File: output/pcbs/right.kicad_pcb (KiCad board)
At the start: 2 copper layers, 140.2 x 118.9 mm, 62 parts

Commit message: PCB config is now mostly completed
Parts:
- moved D1 264.6 mm to (364.6, 88.0)
- moved D2 264.6 mm to (364.6, 71.0)
- moved D3 264.6 mm to (364.6, 54.0)
- moved D4 264.6 mm to (364.6, 37.0)
- moved S1 264.6 mm to (364.6, 83.0)
- moved S2 264.6 mm to (364.6, 66.0)
- moved S3 264.6 mm to (364.6, 49.0)
- moved S4 264.6 mm to (364.6, 32.0)
- moved D5 219.6 mm to (342.1, 88.0)
- moved D6 219.6 mm to (342.1, 71.0)
- moved D7 219.6 mm to (342.1, 54.0)
- moved D8 219.6 mm to (342.1, 37.0)
- moved S5 219.6 mm to (342.1, 83.0)
- moved S6 219.6 mm to (342.1, 66.0)
- moved S7 219.6 mm to (342.1, 49.0)
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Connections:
- net extra_cluster renamed mirror_extra_cluster
- net index_bottom renamed mirror_index_bottom
- net index_home renamed mirror_index_home
- net index_mod renamed mirror_index_mod
- net index_num renamed mirror_index_num
- net index_top renamed mirror_index_top
- net inner_bottom renamed mirror_inner_bottom
- net inner_home renamed mirror_inner_home
- net inner_num renamed mirror_inner_num
- net inner_top renamed mirror_inner_top
- net middle_bottom renamed mirror_middle_bottom
- net middle_home renamed mirror_middle_home
- net middle_mod renamed mirror_middle_mod
- net middle_num renamed mirror_middle_num
- net middle_top renamed mirror_middle_top
- net outer_bottom renamed mirror_outer_bottom
- net outer_home renamed mirror_outer_home
- net outer_num renamed mirror_outer_num
- net outer_top renamed mirror_outer_top
- net pinky_bottom renamed mirror_pinky_bottom
- net pinky_home renamed mirror_pinky_home
- net pinky_num renamed mirror_pinky_num
- net pinky_top renamed mirror_pinky_top
- net ring_bottom renamed mirror_ring_bottom
- net ring_home renamed mirror_ring_home
- net ring_mod renamed mirror_ring_mod
- net ring_num renamed mirror_ring_num
- net ring_top renamed mirror_ring_top
- net space_cluster renamed mirror_space_cluster
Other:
- outline, holes or cut-outs redrawn

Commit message: A bit more touch-up on the PCB.  Things are shaping up, but not yet done.
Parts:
- added ROT1: , rotary_encoder, F.Cu at (251.6, 70.5)
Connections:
- D28 pad 1: (no net) -> P113
- D29 pad 1: (no net) -> P113
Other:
- board text added: "CYBERFOX-60"
- board text removed: "CYBERFOX"

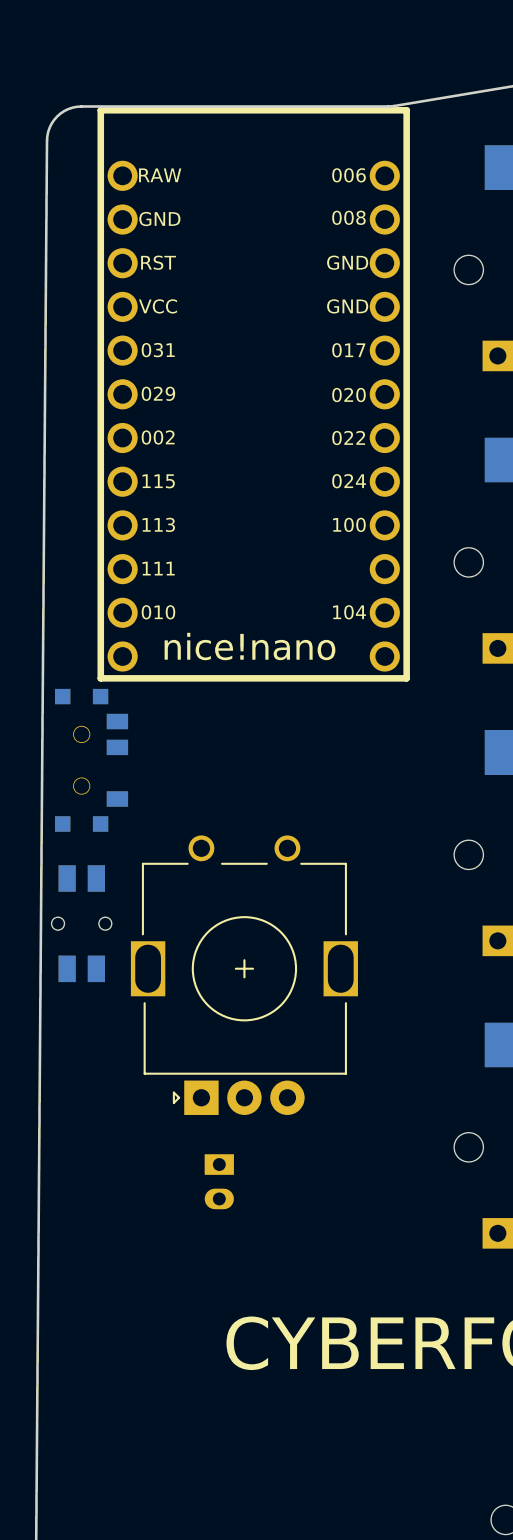
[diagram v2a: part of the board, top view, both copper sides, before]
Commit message: Changed from rotary knob to scrollwheel. Further minor refinements.
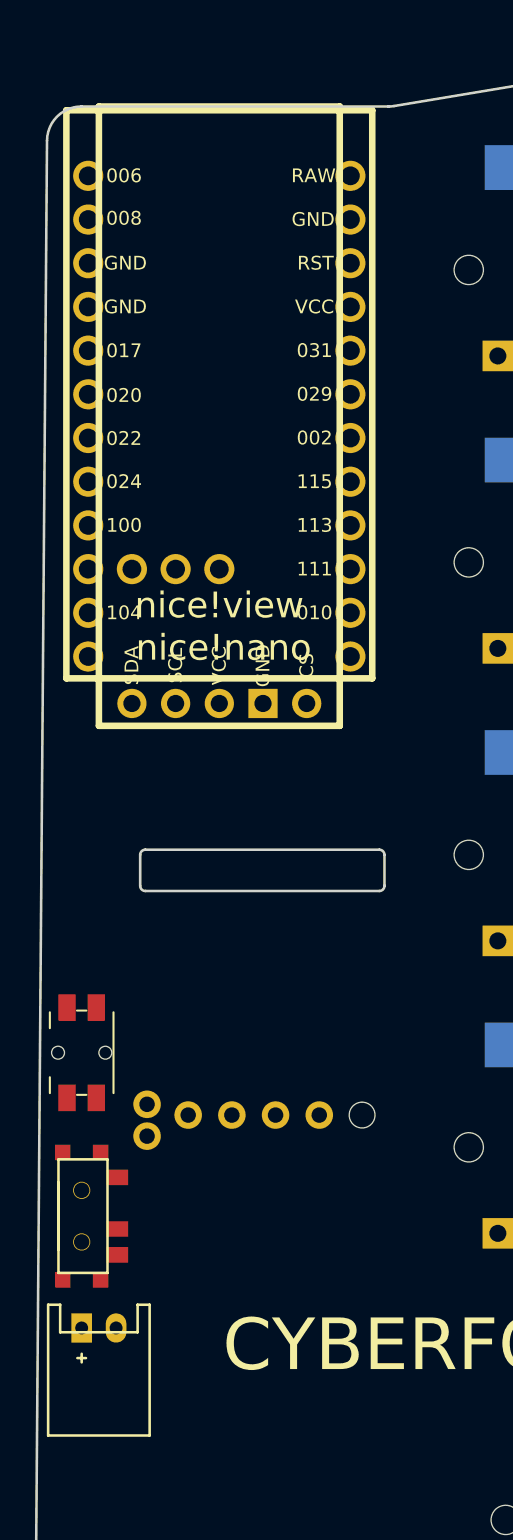
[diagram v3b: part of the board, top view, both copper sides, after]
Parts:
- removed ROT1: , rotary_encoder
- added REF**: RollerEncoder_Panasonic_EVQWGD001, RollerEncoder_Panasonic_EVQWGD001, F.Cu at (252.1, 73.5)
- added niceView1: niceView, lib:niceView_headers, F.Cu at (250.1, 56.5)
- moved T1 26.5 mm to (242.1, 85.0)
- moved JST1 11.0 mm to (243.1, 91.5), turned to 0 degrees
- moved B1 7.50 mm to (242.1, 75.5)
- moved MCU1 2.00 mm to (250.1, 38.5)
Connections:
- net pos renamed POS
- D13 pad 1: P013 -> P031
- D18 pad 1: P013 -> P031
- D23 pad 1: P013 -> P031
- D27 pad 1: P013 -> P031
- D4 pad 1: P013 -> P031
- D8 pad 1: P013 -> P031
- S1 pad 1: P020 -> P011
- S10 pad 1: P024 -> P106
- S11 pad 1: P024 -> P106
- S12 pad 1: P024 -> P106
- S13 pad 1: P024 -> P106
- S14 pad 1: P024 -> P106
- S15 pad 1: P100 -> P111
- S16 pad 1: P100 -> P111
- S17 pad 1: P100 -> P111
- S18 pad 1: P100 -> P111
- S19 pad 1: P100 -> P111
- S2 pad 1: P020 -> P011
- S20 pad 1: P011 -> P010
- S21 pad 1: P011 -> P010
- S22 pad 1: P011 -> P010
- S23 pad 1: P011 -> P010
- S24 pad 1: P017 -> P009
- S25 pad 1: P017 -> P009
- S26 pad 1: P017 -> P009
- S27 pad 1: P017 -> P009
- S28 pad 1: P011 -> P010
- S29 pad 1: P017 -> P009
- S3 pad 1: P020 -> P011
- S4 pad 1: P020 -> P011
- S5 pad 1: P022 -> P104
- S6 pad 1: P022 -> P104
- S7 pad 1: P022 -> P104
- S8 pad 1: P022 -> P104
- S9 pad 1: P022 -> P104

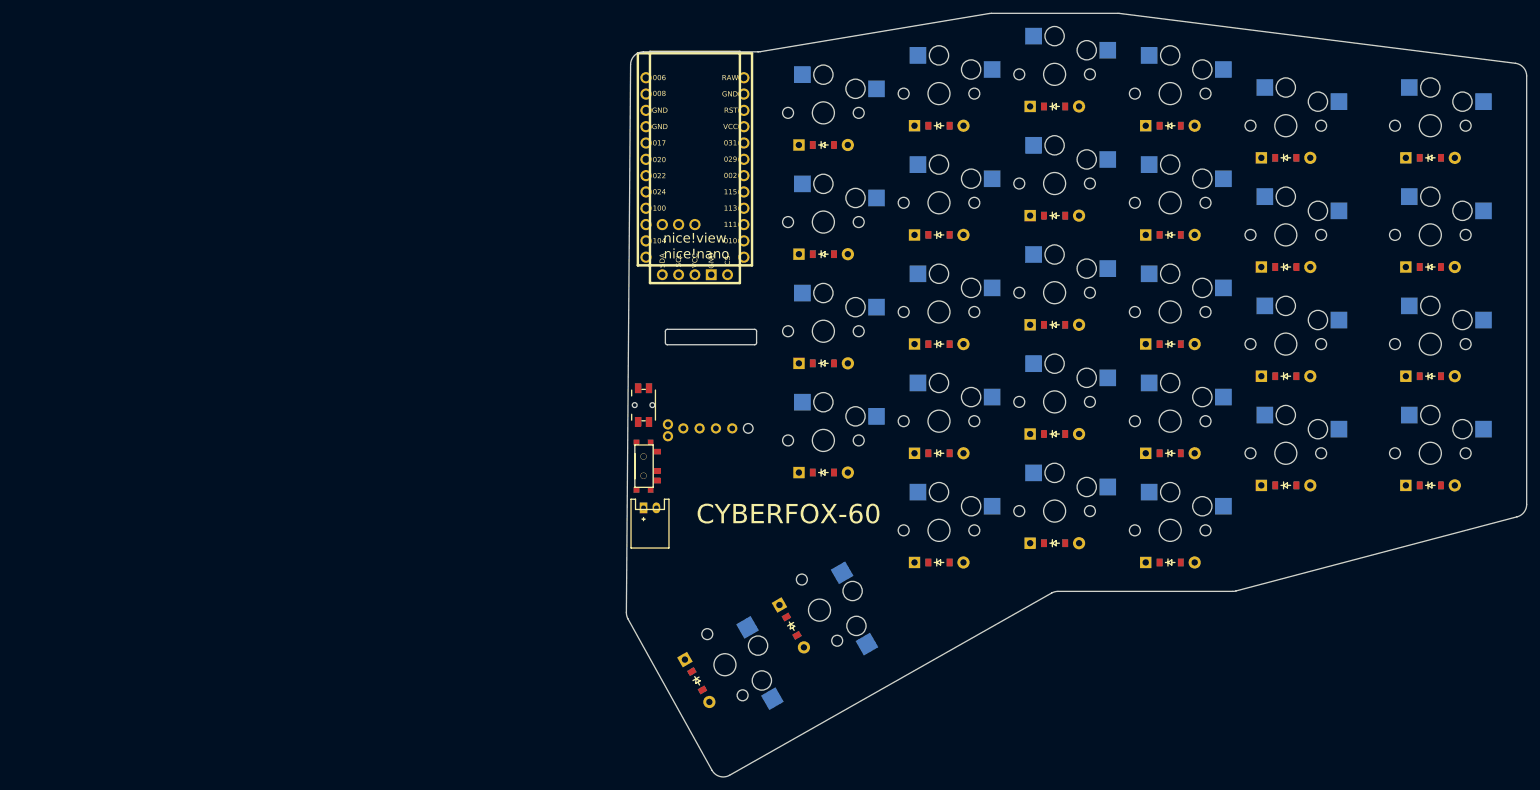
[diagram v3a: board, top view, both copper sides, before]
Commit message: Added screw holes and an extra diode for the scrollwheel
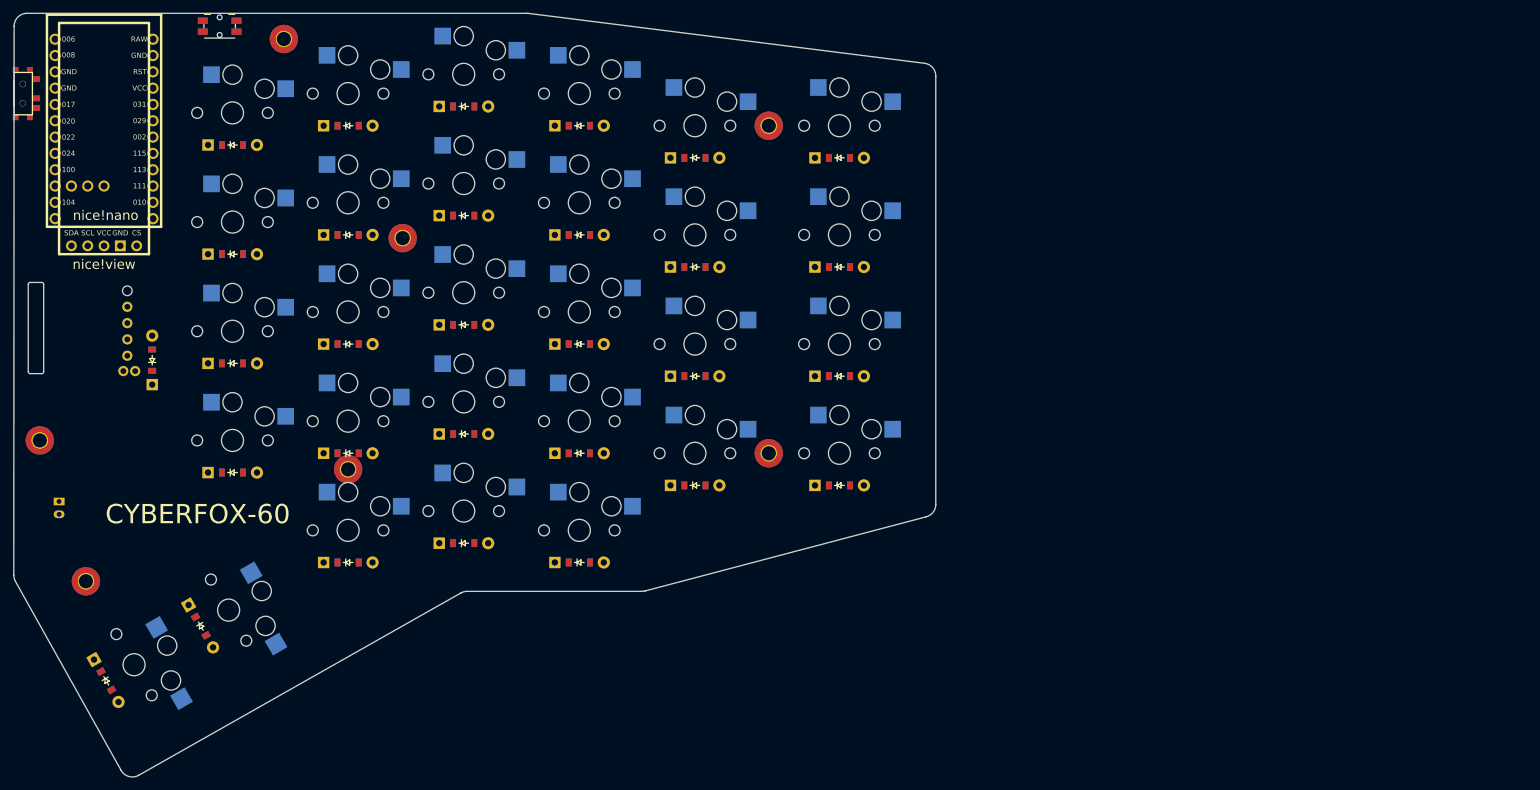
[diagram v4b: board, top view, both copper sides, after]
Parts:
- added D30: , ComboDiode, F.Cu at (165.6, 68.5)
- added _2: , HOLE_M2, F.Cu at (155.3, 102.9)
- added _3: , HOLE_M2, F.Cu at (148.1, 81.0)
- added _4: , HOLE_M2, F.Cu at (186.1, 18.5)
- added _5: , HOLE_M2, F.Cu at (261.6, 32.0)
- added _6: , HOLE_M2, F.Cu at (261.6, 83.0)
- added _7: , HOLE_M2, F.Cu at (204.6, 49.5)
- added _8: , HOLE_M2, F.Cu at (196.1, 85.5)
- REF**: value RollerEncoder_Panasonic_EVQWGD001 -> EVQWGD001
- moved T1 112.7 mm to (145.5, 27.0)
- moved REF** 96.5 mm to (156.1, 64.0), turned to -180 degrees
- moved MCU1 92.2 mm to (158.1, 32.5)
- moved niceView1 92.1 mm to (158.1, 52.0)
- moved D1 92.0 mm to (272.6, 88.0)
- moved D10 92.0 mm to (232.1, 83.0)
- moved D11 92.0 mm to (232.1, 66.0)
- moved D12 92.0 mm to (232.1, 49.0)
- moved D13 92.0 mm to (232.1, 32.0)
- moved D14 92.0 mm to (214.1, 97.0)
- moved D15 92.0 mm to (214.1, 80.0)
- moved D16 92.0 mm to (214.1, 63.0)
- moved D17 92.0 mm to (214.1, 46.0)
- moved D18 92.0 mm to (214.1, 29.0)
- moved D19 92.0 mm to (196.1, 100.0)
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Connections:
- REF** pad S2: P113 -> ROTARY
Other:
- board size 140.2 x 118.9 mm -> 143.6 x 118.9 mm

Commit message: Starting to trace the PCB
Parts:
- moved _8 47.3 mm to (231.9, 116.5)
- moved D1 39.1 mm to (310.6, 97.2)
- moved D5 39.1 mm to (288.1, 97.2)
- moved S1 39.1 mm to (310.6, 92.2)
- moved S5 39.1 mm to (288.1, 92.2)
- moved D2 38.9 mm to (310.6, 79.5)
- moved D6 38.9 mm to (288.1, 79.5)
- moved S2 38.9 mm to (310.6, 74.5)
- moved S6 38.9 mm to (288.1, 74.5)
- moved D3 38.8 mm to (310.6, 61.8)
- moved D7 38.8 mm to (288.1, 61.8)
- moved S3 38.8 mm to (310.6, 56.8)
- moved S7 38.8 mm to (288.1, 56.8)
- moved D4 38.6 mm to (310.6, 44.0)
- moved D8 38.6 mm to (288.1, 44.0)
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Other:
- board size 143.6 x 118.9 mm -> 149.7 x 121.9 mm
